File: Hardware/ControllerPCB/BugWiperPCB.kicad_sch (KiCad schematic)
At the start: 13 parts, among them J2 1770924, J3 Phoenix_1776508, J6 1824420000, J7 Conn_01x02_Pin

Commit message: Export schematics
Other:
- company: (none) -> M. Scholjegerdes
- title: (none) -> BugWiper 2.0 Controller PCB
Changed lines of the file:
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@@
 (kicad_sch (version 20230121) (generator eeschema)
   (paper "A4")
+  (title_block
+    (title "BugWiper 2.0 Controller PCB")
+    (date "2025-01-27")
+    (company "M. Scholjegerdes")
+  )
   (junction (at 114.3 176.53) (diameter 0) (color 0 0 0 0)
   )

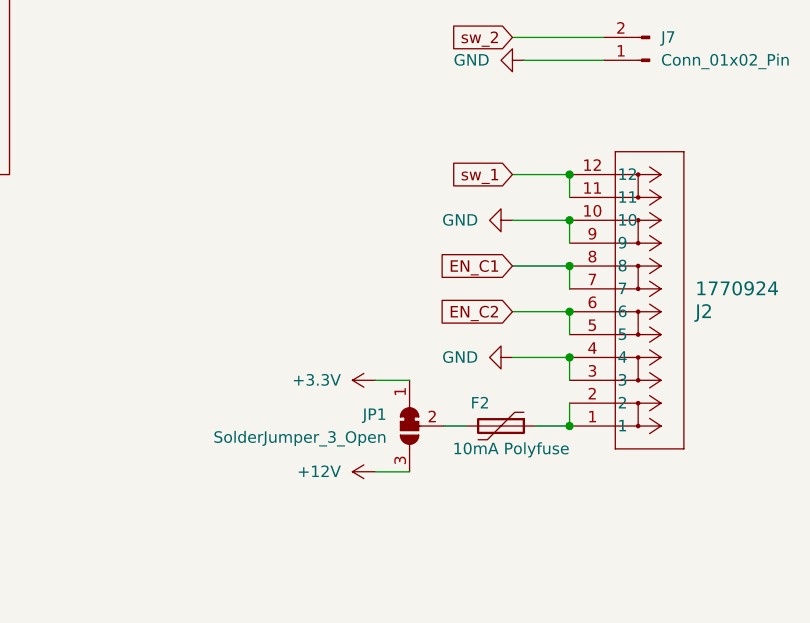
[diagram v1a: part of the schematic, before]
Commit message: update Controller PCB
Add Fuses for GND Signal Connectors, fix 3D and fix DRC
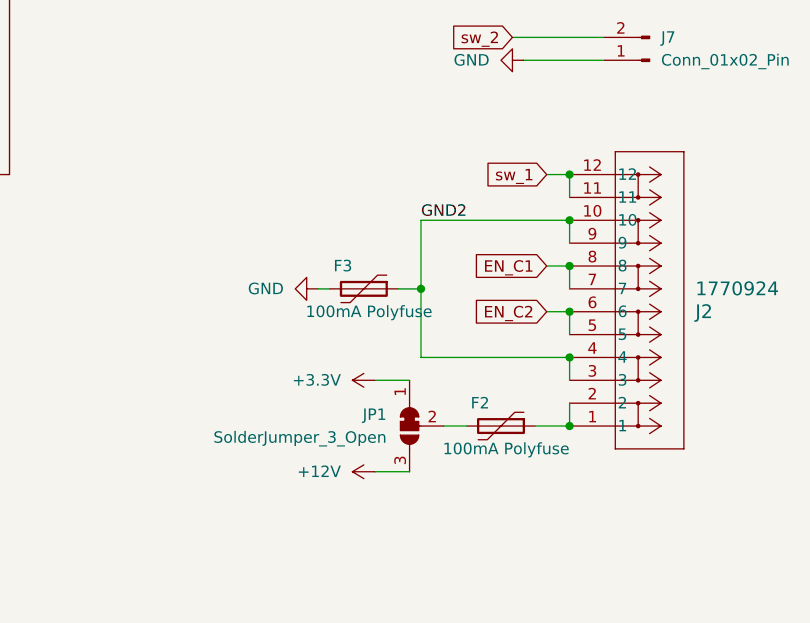
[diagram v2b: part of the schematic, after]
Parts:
- added F3: 100mA Polyfuse, Resistor_SMD:R_1206_3216Metric, symbol Device:Polyfuse
- F2: value 10mA Polyfuse -> 100mA Polyfuse; Manufacturer_Name (none) -> Eaton Electronics; Manufacturer_Part_Number (none) -> PTS120630V012; Price (none) -> 0,108€
- H1, H2, H3, H4: footprint MountingHole:MountingHole_3.2mm_M3_DIN965 -> MountingHole:MountingHole_3.2mm_M3_DIN965_Pad
- J3: Manufacturer_Name (none) -> Phoenix Contact
- J6: footprint SHDR4W80P700X350_2X2_770X1400X850P -> BugWiper_lib:SHDR4W80P700X350_2X2_770X1400X850P
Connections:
- net GND: now also F3.2; no longer J2.10, J2.3, J2.4, J2.9
- new net GND2: F3.1, J2.10, J2.3, J2.4, J2.9
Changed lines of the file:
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@@
     (company "M. Scholjegerdes")
   )
+  (junction (at 226.06 128.27) (diameter 0) (color 0 0 0 0)
+  )
   (junction (at 114.3 176.53) (diameter 0) (color 0 0 0 0)
   )
@@
     (stroke (width 0) (type default))
   )
+  (wire (pts (xy 223.52 128.27) (xy 226.06 128.27))
+    (stroke (width 0) (type default))
+  )
   (wire (pts (xy 72.39 90.17) (xy 76.2 90.17))
     (stroke (width 0) (type default))
   )
-  (wire (pts (xy 236.22 135.89) (xy 242.57 135.89))
+  (wire (pts (xy 214.63 128.27) (xy 215.9 128.27))
     (stroke (width 0) (type default))
   )
@@
     (stroke (width 0) (type default))
   )
+  (wire (pts (xy 226.06 120.65) (xy 226.06 128.27))
+    (stroke (width 0) (type default))
+  )
+  (wire (pts (xy 226.06 135.89) (xy 242.57 135.89))
+    (stroke (width 0) (type default))
+  )
   (wire (pts (xy 116.84 87.63) (xy 142.24 87.63))
     (stroke (width 0) (type default))
@@
     (stroke (width 0) (type default))
   )
-  (wire (pts (xy 236.22 120.65) (xy 242.57 120.65))
+  (wire (pts (xy 226.06 120.65) (xy 242.57 120.65))
     (stroke (width 0) (type default))
   )
@@
     (stroke (width 0) (type default))
   )
-  (wire (pts (xy 236.22 130.81) (xy 242.57 130.81))
+  (wire (pts (xy 240.03 130.81) (xy 242.57 130.81))
     (stroke (width 0) (type default))
   )
@@
     (stroke (width 0) (type default))
   )
-  (wire (pts (xy 236.22 115.57) (xy 242.57 115.57))
+  (wire (pts (xy 240.03 115.57) (xy 242.57 115.57))
     (stroke (width 0) (type default))
   )
@@
     (stroke (width 0) (type default))
   )
-  (wire (pts (xy 236.22 125.73) (xy 242.57 125.73))
+  (wire (pts (xy 240.03 125.73) (xy 242.57 125.73))
     (stroke (width 0) (type default))
   )
@@
     (stroke (width 0) (type default))
   )
+  (wire (pts (xy 226.06 128.27) (xy 226.06 135.89))
+    (stroke (width 0) (type default))
+  )
   (wire (pts (xy 128.27 62.23) (xy 142.24 62.23))
     (stroke (width 0) (type default))
@@
     (fill (type none))
   )
-  (global_label "EN_C1" (shape input) (at 236.22 125.73 180) (fields_autoplaced)
+  (label "GND2" (at 226.06 120.65 0) (fields_autoplaced)
+    (effects (font (size 1.27 1.27)) (justify left bottom))
+  )
+  (global_label "EN_C1" (shape input) (at 240.03 125.73 180) (fields_autoplaced)
     (effects (font (size 1.27 1.27)) (justify right))
-    (property "Intersheetrefs" "${INTERSHEET_REFS}" (at 227.3082 125.73 0)
+    (property "Intersheetrefs" "${INTERSHEET_REFS}" (at 231.1182 125.73 0)
       (effects (font (size 1.27 1.27)) (justify right) hide)
     )
@@
     )
   )
-  (global_label "EN_C2" (shape input) (at 236.22 130.81 180) (fields_autoplaced)
+  (global_label "EN_C2" (shape input) (at 240.03 130.81 180) (fields_autoplaced)
     (effects (font (size 1.27 1.27)) (justify right))
-    (property "Intersheetrefs" "${INTERSHEET_REFS}" (at 227.3082 130.81 0)
+    (property "Intersheetrefs" "${INTERSHEET_REFS}" (at 231.1182 130.81 0)
       (effects (font (size 1.27 1.27)) (justify right) hide)
     )
   )
-  (global_label "sw_1" (shape input) (at 236.22 115.57 180) (fields_autoplaced)
+  (global_label "sw_1" (shape input) (at 240.03 115.57 180) (fields_autoplaced)
     (effects (font (size 1.27 1.27)) (justify right))
-    (property "Intersheetrefs" "${INTERSHEET_REFS}" (at 228.6991 115.57 0)
+    (property "Intersheetrefs" "${INTERSHEET_REFS}" (at 232.5091 115.57 0)
       (effects (font (size 1.27 1.27)) (justify right) hide)
     )
@@
     (property "Intersheetrefs" "${INTERSHEET_REFS}" (at 63.4782 82.55 0)
       (effects (font (size 1.27 1.27)) (justify right) hide)
+    )
+  )
+  (symbol (lib_id "Device:Polyfuse") (at 219.71 128.27 270) (unit 1)
+    (in_bom yes) (on_board yes) (dnp no)
+    (property "Reference" "F3" (at 218.44 125.73 90)
+      (effects (font (size 1.27 1.27)) (justify right))
+    )
+    (property "Value" "100mA Polyfuse" (at 227.33 130.81 90)
+      (effects (font (size 1.27 1.27)) (justify right))
+    )
+    (property "Footprint" "Resistor_SMD:R_1206_3216Metric" (at 214.63 129.54 0)
+      (effects (font (size 1.27 1.27)) (justify left) hide)
+    )
+    (property "Datasheet" "https://eu.mouser.com/datasheet/2/87/eaton_pts1206_6_60_volt_dc_surface_mount_resettabl-1608737.pdf" (at 219.71 128.27 0)
+      (effects (font (size 1.27 1.27)) hide)
+    )
+    (property "Description" "100mA resettable FUSE" (at 219.71 128.27 0)
+      (effects (font (size 1.27 1.27)) hide)
+    )
+    (property "Manufacturer_Name" "Eaton Electronics" (at 219.71 128.27 0)
+      (effects (font (size 1.27 1.27)) hide)
+    )
+    (property "Manufacturer_Part_Number" "PTS120630V012" (at 219.71 128.27 0)
+      (effects (font (size 1.27 1.27)) hide)
+    )
+    (property "Price" "0,108€" (at 219.71 128.27 0)
+      (effects (font (size 1.27 1.27)) hide)
+    )
+    (pin "1")
+    (pin "2")
+    (instances
+      (project "BugWiperPCB"
+        (path "/d31a15bd-db02-4d4c-9593-17c596d3182c"
+          (reference "F3") (unit 1)
+        )
+      )
     )
   )
@@
       (effects (font (size 1.27 1.27)) (justify bottom) hide)
     )
+    (property "Manufacturer_Name" "Phoenix Contact" (at 156.21 43.18 0)
+      (effects (font (size 1.27 1.27)) hide)
+    )
     (pin "1")
     (pin "2")
@@
       (effects (font (size 1.27 1.27)) (justify right))
     )
-    (property "Value" "10mA Polyfuse" (at 242.57 146.05 90)
+    (property "Value" "100mA Polyfuse" (at 242.57 146.05 90)
       (effects (font (size 1.27 1.27)) (justify right))
     )
@@
       (effects (font (size 1.27 1.27)) (justify left) hide)
     )
-    (property "Datasheet" "~" (at 234.95 143.51 0)
+    (property "Datasheet" "https://eu.mouser.com/datasheet/2/87/eaton_pts1206_6_60_volt_dc_surface_mount_resettabl-1608737.pdf" (at 234.95 143.51 0)
+      (effects (font (size 1.27 1.27)) hide)
+    )
+    (property "Description" "100mA resettable FUSE" (at 234.95 143.51 0)
+      (effects (font (size 1.27 1.27)) hide)
+    )
+    (property "Manufacturer_Name" "Eaton Electronics" (at 234.95 143.51 0)
+      (effects (font (size 1.27 1.27)) hide)
+    )
+    (property "Manufacturer_Part_Number" "PTS120630V012" (at 234.95 143.51 0)
+      (effects (font (size 1.27 1.27)) hide)
+    )
+    (property "Price" "0,108€" (at 234.95 143.51 0)
       (effects (font (size 1.27 1.27)) hide)
     )
@@
       (effects (font (size 1.27 1.27)) (justify left))
     )
-    (property "Footprint" "MountingHole:MountingHole_3.2mm_M3_DIN965" (at 114.3 144.78 0)
+    (property "Footprint" "MountingHole:MountingHole_3.2mm_M3_DIN965_Pad" (at 114.3 144.78 0)
       (effects (font (size 1.27 1.27)) hide)
     )
@@
       (effects (font (size 1.27 1.27)) (justify left))
     )
-    (property "Footprint" "MountingHole:MountingHole_3.2mm_M3_DIN965" (at 48.26 144.78 0)
+    (property "Footprint" "MountingHole:MountingHole_3.2mm_M3_DIN965_Pad" (at 48.26 144.78 0)
       (effects (font (size 1.27 1.27)) hide)
     )
@@
     )
   )
-  (symbol (lib_id "power:GND") (at 236.22 120.65 270) (unit 1)
-    (in_bom yes) (on_board yes) (dnp no) (fields_autoplaced)
-    (property "Reference" "#PWR073" (at 229.87 120.65 0)
-      (effects (font (size 1.27 1.27)) hide)
-    )
-    (property "Value" "GND" (at 232.41 120.65 90)
-      (effects (font (size 1.27 1.27)) (justify right))
-    )
-    (property "Footprint" "" (at 236.22 120.65 0)
-      (effects (font (size 1.27 1.27)) hide)
-    )
-    (property "Datasheet" "" (at 236.22 120.65 0)
-      (effects (font (size 1.27 1.27)) hide)
-    )
-    (pin "1")
-    (instances
-      (project "BugWiperPCB"
-        (path "/d31a15bd-db02-4d4c-9593-17c596d3182c"
-          (reference "#PWR073") (unit 1)
-        )
-      )
-    )
-  )
   (symbol (lib_id "Mechanical:MountingHole_Pad") (at 114.3 163.83 0) (unit 1)
     (in_bom yes) (on_board yes) (dnp no) (fields_autoplaced)
@@
       (effects (font (size 1.27 1.27)) (justify left))
     )
-    (property "Footprint" "MountingHole:MountingHole_3.2mm_M3_DIN965" (at 82.55 144.78 0)
+    (property "Footprint" "MountingHole:MountingHole_3.2mm_M3_DIN965_Pad" (at 82.55 144.78 0)
       (effects (font (size 1.27 1.27)) hide)
     )
@@
       (effects (font (size 1.27 1.27)))
     )
-    (property "Footprint" "SHDR4W80P700X350_2X2_770X1400X850P" (at 204.47 180.01 0)
+    (property "Footprint" "BugWiper_lib:SHDR4W80P700X350_2X2_770X1400X850P" (at 204.47 180.01 0)
       (effects (font (size 1.27 1.27)) (justify left top) hide)
     )
@@
       (effects (font (size 1.27 1.27)) (justify left))
     )
-    (property "Footprint" "MountingHole:MountingHole_3.2mm_M3_DIN965" (at 48.26 162.56 0)
+    (property "Footprint" "MountingHole:MountingHole_3.2mm_M3_DIN965_Pad" (at 48.26 162.56 0)
       (effects (font (size 1.27 1.27)) hide)
     )
@@
     )
   )
-  (symbol (lib_id "power:GND") (at 236.22 135.89 270) (unit 1)
-    (in_bom yes) (on_board yes) (dnp no) (fields_autoplaced)
-    (property "Reference" "#PWR074" (at 229.87 135.89 0)
-      (effects (font (size 1.27 1.27)) hide)
-    )
-    (property "Value" "GND" (at 232.41 135.89 90)
-      (effects (font (size 1.27 1.27)) (justify right))
-    )
-    (property "Footprint" "" (at 236.22 135.89 0)
-      (effects (font (size 1.27 1.27)) hide)
-    )
-    (property "Datasheet" "" (at 236.22 135.89 0)
-      (effects (font (size 1.27 1.27)) hide)
-    )
+  (symbol (lib_id "power:GND") (at 214.63 128.27 270) (unit 1)
+    (in_bom yes) (on_board yes) (dnp no) (fields_autoplaced)
+    (property "Reference" "#PWR074" (at 208.28 128.27 0)
+      (effects (font (size 1.27 1.27)) hide)
+    )
+    (property "Value" "GND" (at 210.82 128.27 90)
+      (effects (font (size 1.27 1.27)) (justify right))
+    )
+    (property "Footprint" "" (at 214.63 128.27 0)
+      (effects (font (size 1.27 1.27)) hide)
+    )
+    (property "Datasheet" "" (at 214.63 128.27 0)
+      (effects (font (size 1.27 1.27)) hide)
+    )

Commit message: Update PCB
Add solder jumper for +3.3V selection
fix DRC
aligne vias
export Gerber
add text
fix 3D Models
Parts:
- J7: footprint Connector_JST:JST_XH_B2B-XH-AM_1x02_P2.50mm_Vertical -> BugWiper_lib:JST_XH_B2B-XH-AM_1x02_P2.50mm_Vertical
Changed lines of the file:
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@@
       (effects (font (size 1.27 1.27)) (justify right))
     )
-    (property "Footprint" "Connector_JST:JST_XH_B2B-XH-AM_1x02_P2.50mm_Vertical" (at 251.46 102.87 0)
+    (property "Footprint" "BugWiper_lib:JST_XH_B2B-XH-AM_1x02_P2.50mm_Vertical" (at 251.46 102.87 0)
       (effects (font (size 1.27 1.27)) hide)
     )

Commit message: update Controller PCB
Add additional capacitor
fix footprint Resistor Array CAT16
fix 3D Model CAT16
change traces from 0.5 to 0.4 mm
fix USB-C Footprint
Export Gerber
update BOM and Values
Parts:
- J3: STANDARD Manufacturer Recommendations -> (none)
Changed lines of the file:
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@@
+      (effects (font (size 1.27 1.27)) hide)
+    )
+    (property "Alternative MF" "" (at 219.71 128.27 0)
+      (effects (font (size 1.27 1.27)) hide)
+    )
+    (property "Alternative PN" "" (at 219.71 128.27 0)
+      (effects (font (size 1.27 1.27)) hide)
+    )
+    (property "Alternative Price" "" (at 219.71 128.27 0)
       (effects (font (size 1.27 1.27)) hide)
     )
@@
       (effects (font (size 1.27 1.27) italic) hide)
     )
+    (property "Alternative MF" "" (at 242.57 143.51 0)
+      (effects (font (size 1.27 1.27)) hide)
+    )
+    (property "Alternative PN" "" (at 242.57 143.51 0)
+      (effects (font (size 1.27 1.27)) hide)
+    )
+    (property "Alternative Price" "" (at 242.57 143.51 0)
+      (effects (font (size 1.27 1.27)) hide)
+    )
     (pin "7")
     (pin "5")
@@
       (effects (font (size 1.27 1.27)) hide)
     )
+    (property "Alternative MF" "" (at 224.79 143.51 0)
+      (effects (font (size 1.27 1.27)) hide)
+    )
+    (property "Alternative PN" "" (at 224.79 143.51 0)
+      (effects (font (size 1.27 1.27)) hide)
+    )
+    (property "Alternative Price" "" (at 224.79 143.51 0)
+      (effects (font (size 1.27 1.27)) hide)
+    )
     (pin "1")
     (pin "3")
@@
       (effects (font (size 1.27 1.27)) (justify bottom) hide)
     )
-    (property "STANDARD" "Manufacturer Recommendations" (at 151.13 43.18 0)
+    (property "STANDARD" "" (at 151.13 43.18 0)
       (effects (font (size 1.27 1.27)) (justify bottom) hide)
     )
@@
     )
     (property "Manufacturer_Name" "Phoenix Contact" (at 156.21 43.18 0)
+      (effects (font (size 1.27 1.27)) hide)
+    )
+    (property "Alternative MF" "" (at 156.21 43.18 0)
+      (effects (font (size 1.27 1.27)) hide)
+    )
+    (property "Alternative PN" "" (at 156.21 43.18 0)
+      (effects (font (size 1.27 1.27)) hide)
+    )
+    (property "Alternative Price" "" (at 156.21 43.18 0)
       (effects (font (size 1.27 1.27)) hide)
     )
@@
       (effects (font (size 1.27 1.27)) hide)
     )
+    (property "Alternative MF" "" (at 234.95 143.51 0)
+      (effects (font (size 1.27 1.27)) hide)
+    )
+    (property "Alternative PN" "" (at 234.95 143.51 0)
+      (effects (font (size 1.27 1.27)) hide)
+    )
+    (property "Alternative Price" "" (at 234.95 143.51 0)
+      (effects (font (size 1.27 1.27)) hide)
+    )
     (pin "1")
     (pin "2")
@@
     )
     (property "Datasheet" "~" (at 114.3 144.78 0)
+      (effects (font (size 1.27 1.27)) hide)
+    )
+    (property "Alternative MF" "" (at 114.3 144.78 0)
+      (effects (font (size 1.27 1.27)) hide)
+    )
+    (property "Alternative PN" "" (at 114.3 144.78 0)
+      (effects (font (size 1.27 1.27)) hide)
+    )
+    (property "Alternative Price" "" (at 114.3 144.78 0)
       (effects (font (size 1.27 1.27)) hide)
     )
@@
       (effects (font (size 1.27 1.27)) hide)
     )
+    (property "Alternative MF" "" (at 251.46 102.87 0)
+      (effects (font (size 1.27 1.27)) hide)
+    )
+    (property "Alternative PN" "" (at 251.46 102.87 0)
+      (effects (font (size 1.27 1.27)) hide)
+    )
+    (property "Alternative Price" "" (at 251.46 102.87 0)
+      (effects (font (size 1.27 1.27)) hide)
+    )
     (pin "1")
     (pin "2")
@@
     )
     (property "Datasheet" "~" (at 48.26 144.78 0)
+      (effects (font (size 1.27 1.27)) hide)
+    )
+    (property "Alternative MF" "" (at 48.26 144.78 0)
+      (effects (font (size 1.27 1.27)) hide)
+    )
+    (property "Alternative PN" "" (at 48.26 144.78 0)
+      (effects (font (size 1.27 1.27)) hide)
+    )
+    (property "Alternative Price" "" (at 48.26 144.78 0)
       (effects (font (size 1.27 1.27)) hide)
     )
@@
       (effects (font (size 1.27 1.27)) hide)
     )
+    (property "Alternative MF" "" (at 110.49 171.45 0)
+      (effects (font (size 1.27 1.27)) hide)
+    )
+    (property "Alternative PN" "" (at 110.49 171.45 0)
+      (effects (font (size 1.27 1.27)) hide)
+    )
+    (property "Alternative Price" "" (at 110.49 171.45 0)
+      (effects (font (size 1.27 1.27)) hide)
+    )
     (pin "2")
     (pin "1")
@@
     )
     (property "Datasheet" "~" (at 114.3 163.83 0)
+      (effects (font (size 1.27 1.27)) hide)
+    )
+    (property "Alternative MF" "" (at 114.3 163.83 0)
+      (effects (font (size 1.27 1.27)) hide)
+    )
+    (property "Alternative PN" "" (at 114.3 163.83 0)
+      (effects (font (size 1.27 1.27)) hide)
+    )
+    (property "Alternative Price" "" (at 114.3 163.83 0)
       (effects (font (size 1.27 1.27)) hide)
     )
@@
       (effects (font (size 1.27 1.27)) hide)
     )
+    (property "Alternative MF" "" (at 82.55 144.78 0)
+      (effects (font (size 1.27 1.27)) hide)
+    )
+    (property "Alternative PN" "" (at 82.55 144.78 0)
+      (effects (font (size 1.27 1.27)) hide)
+    )
+    (property "Alternative Price" "" (at 82.55 144.78 0)
+      (effects (font (size 1.27 1.27)) hide)
+    )
     (instances
       (project "BugWiperPCB"
@@
     )
     (property "Datasheet" "~" (at 114.3 171.45 0)
+      (effects (font (size 1.27 1.27)) hide)
+    )
+    (property "Alternative MF" "" (at 114.3 171.45 0)
+      (effects (font (size 1.27 1.27)) hide)
+    )
+    (property "Alternative PN" "" (at 114.3 171.45 0)
+      (effects (font (size 1.27 1.27)) hide)
+    )
+    (property "Alternative Price" "" (at 114.3 171.45 0)
       (effects (font (size 1.27 1.27)) hide)
     )
@@
       (effects (font (size 1.27 1.27)) (justify left top) hide)
     )
+    (property "Alternative MF" "" (at 187.96 85.09 0)
+      (effects (font (size 1.27 1.27)) hide)
+    )
+    (property "Alternative PN" "" (at 187.96 85.09 0)
+      (effects (font (size 1.27 1.27)) hide)
+    )
+    (property "Alternative Price" "" (at 187.96 85.09 0)
+      (effects (font (size 1.27 1.27)) hide)
+    )
     (pin "3")
     (pin "4")
@@
       (effects (font (size 1.27 1.27)) hide)
     )
+    (property "Alternative MF" "" (at 48.26 162.56 0)
+      (effects (font (size 1.27 1.27)) hide)
+    )
+    (property "Alternative PN" "" (at 48.26 162.56 0)
+      (effects (font (size 1.27 1.27)) hide)
+    )
+    (property "Alternative Price" "" (at 48.26 162.56 0)
+      (effects (font (size 1.27 1.27)) hide)
+    )
